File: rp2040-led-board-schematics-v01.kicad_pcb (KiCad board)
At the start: 4 copper layers, 228 x 98 mm, 293 parts, among them J1 ReceiverRS485, J10 Terminal, J11 ReceiverData, J12 ReceiverData, J13 ReceiverData, J14 ReceiverData, J15 ReceiverRS485, J16 ReceiverRS485, J17 ReceiverRS485, J18 ReceiverRS485, J19 Terminal, J2 ReceiverRS485, J20 Terminal, J21 Terminal, J22 Terminal, J23 ReceiverData, J24 ReceiverData, J25 ReceiverData, J26 ReceiverData, J27 MainBoard, J3 ReceiverRS485, J4 ReceiverRS485, J5 PWR_IN, J6 Terminal, J7 Terminal, J8 Terminal, J9 FrontPanel, Q1 AO3401A, SW1 PEC16, SW2 Button, U10 MAX485EE, U11 MAX485EE, U12 MAX485EE, U13 MAX485EE, U14 Pico, U15 MAX485EE, U16 MAX485EE, U17 AMS1117-5.0, U2 LMR50410Y5FQDBVRQ1, U21 MAX485EE, U22 MAX485EE, U23 MAX485EE, U24 MAX485EE, U25 MAX485EE, U26 MAX485EE, U27 ENC28J60, U29 AMS1117-5.0, U30 AMS1117-5.0, U31 AMS1117-5.0, U32 AMS1117-5.0, U33 AMS1117-5.0, U34 AMS1117-5.0, U35 AMS1117-5.0, U6 MAX485EE, U7 MAX485EE, U8 MAX485EE, U9 MAX485EE

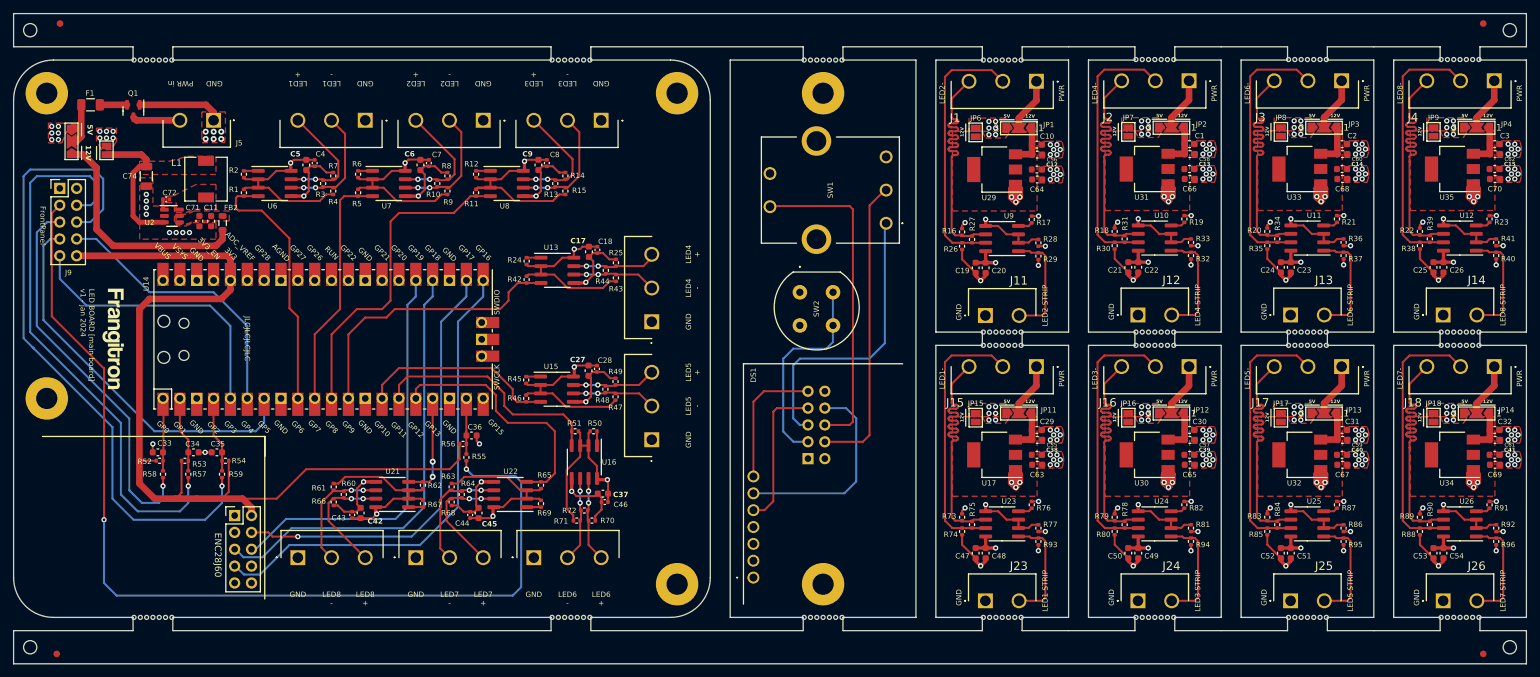
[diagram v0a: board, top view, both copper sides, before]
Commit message: remove designators from silkscreens (manufacturer considers different designs otherwise)
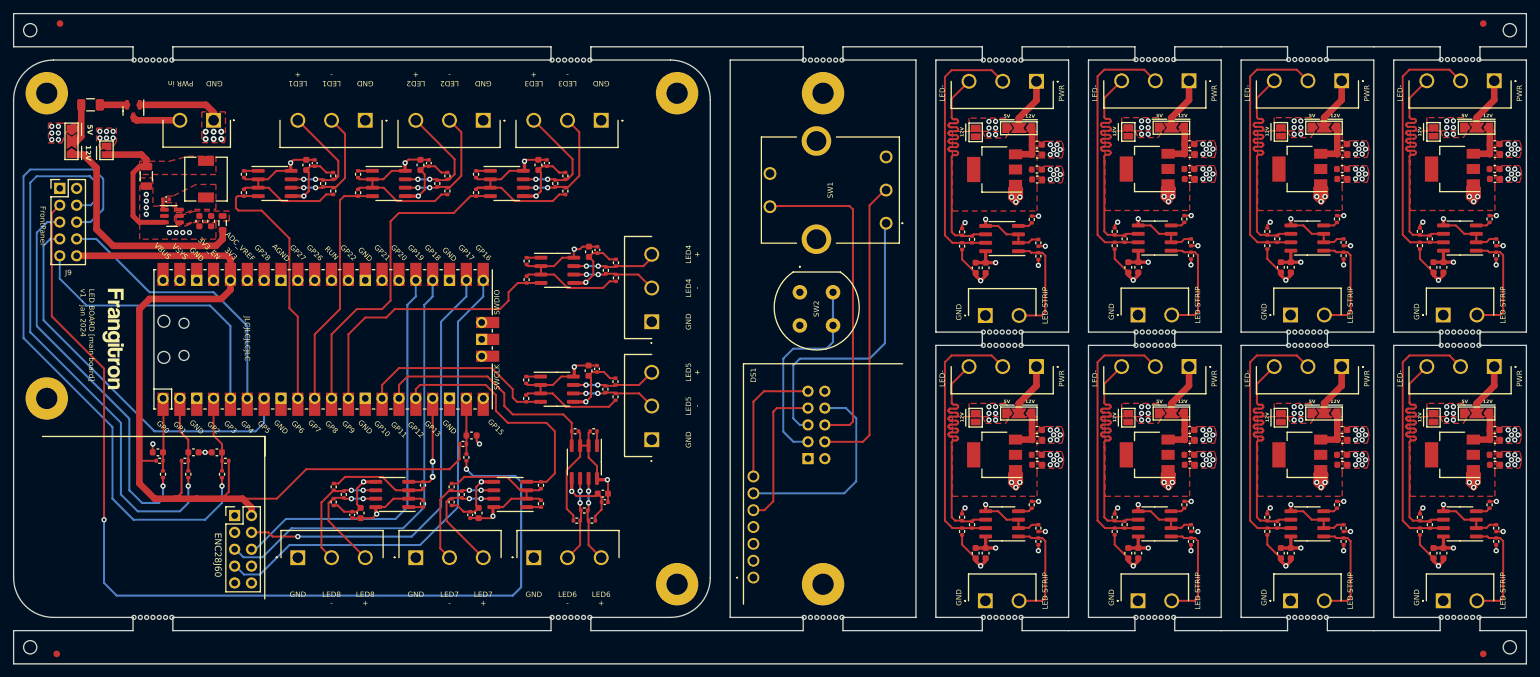
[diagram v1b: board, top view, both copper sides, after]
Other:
- board text added: "LED BOARD [receiver] v1 - jan 2024"
- board text added: "LED STRIP"
- board text added: "LED-"
- board text removed: "LED BOARD [receiver1] v1 - jan 2024"
- board text removed: "LED BOARD [receiver2] v1 - jan 2024"
- board text removed: "LED BOARD [receiver3] v1 - jan 2024"
- board text removed: "LED BOARD [receiver4] v1 - jan 2024"
- board text removed: "LED BOARD [receiver5] v1 - jan 2024"
- board text removed: "LED BOARD [receiver6] v1 - jan 2024"
- board text removed: "LED BOARD [receiver7] v1 - jan 2024"
- board text removed: "LED BOARD [receiver8] v1 - jan 2024"
- board text removed: "LED1 STRIP"
- board text removed: "LED1-"
- board text removed: "LED2 STRIP"
- board text removed: "LED2-"
- board text removed: "LED3 STRIP"
- board text removed: "LED3-"
- board text removed: "LED4 STRIP"
- board text removed: "LED4-"
- board text removed: "LED5 STRIP"
- board text removed: "LED5-"
- board text removed: "LED6 STRIP"
- board text removed: "LED6-"
- board text removed: "LED7 STRIP"
- board text removed: "LED7-"
- board text removed: "LED8 STRIP"
- board text removed: "LED8-"

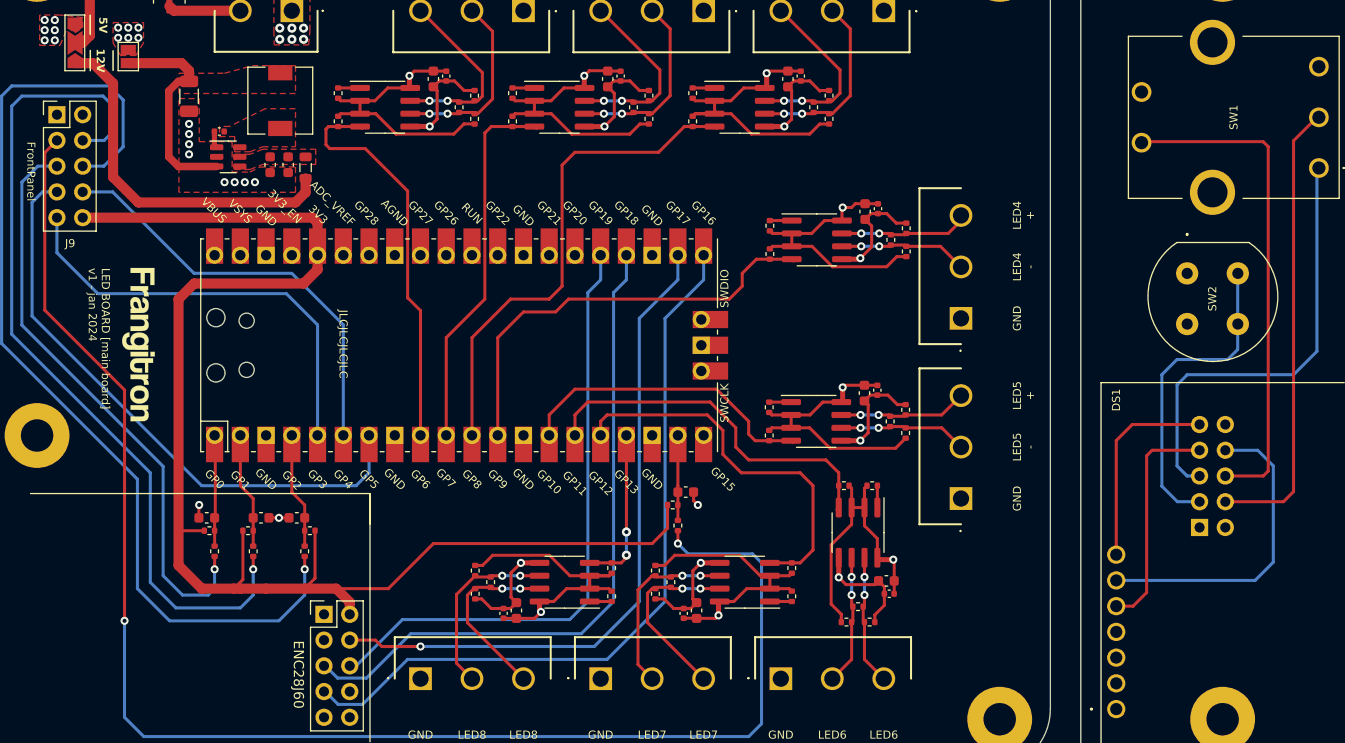
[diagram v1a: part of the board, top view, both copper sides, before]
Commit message: fix: remove designators from silkscreens (forgot some)
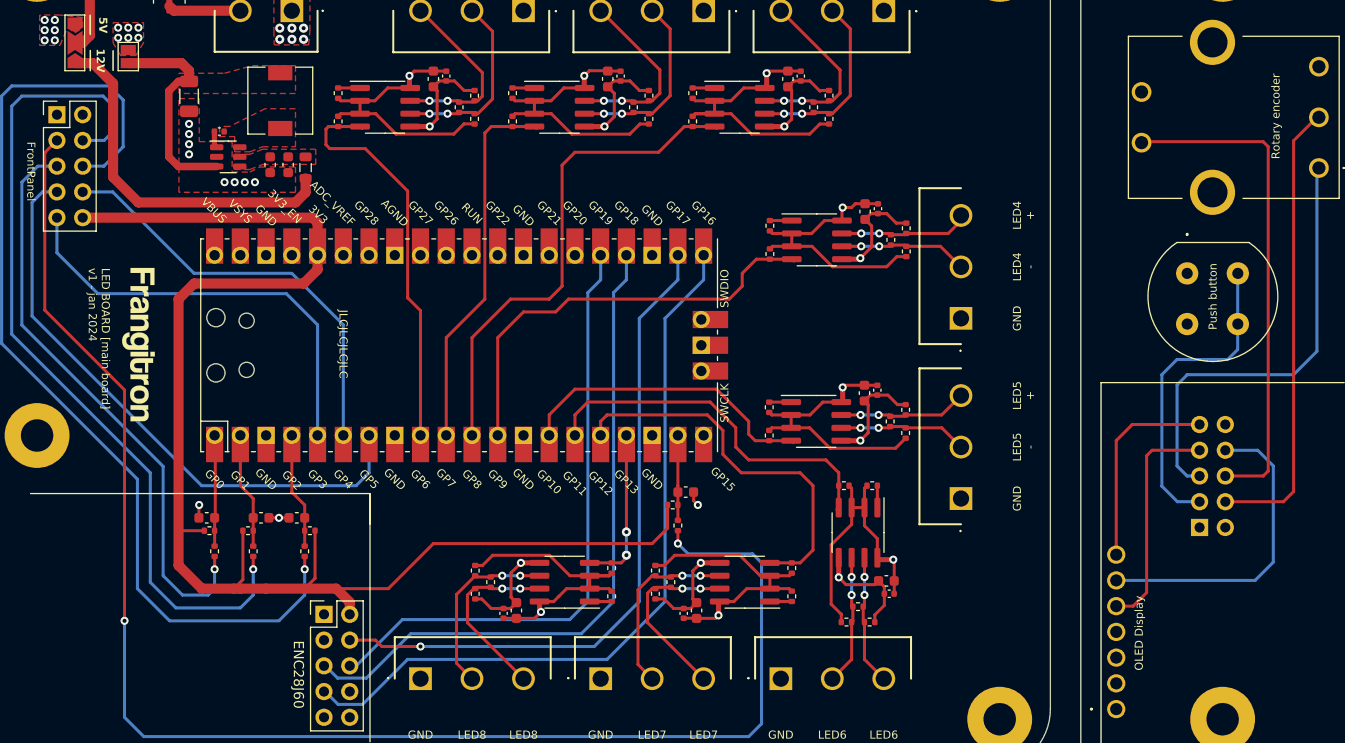
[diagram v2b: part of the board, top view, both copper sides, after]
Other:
- board text added: "OLED Display"
- board text added: "Push button"
- board text added: "Rotary encoder"
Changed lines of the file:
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@@
     (property "ki_keywords" "switch normally-open pushbutton push-button")
     (attr through_hole exclude_from_pos_files)
-    (fp_text reference "SW2" (at 2.5 -2.5 -90) (layer "F.SilkS")
+    (fp_text reference "SW2" (at 2.5 -2.5 -90) (layer "F.SilkS") hide
         (effects (font (size 0.8 0.8) (thickness 0.15)))
     )
@@
     (property "ki_description" "OLED Displays & Accessories")
     (attr through_hole exclude_from_pos_files)
-    (fp_text reference "DS1" (at 30.5 0 90) (layer "F.SilkS")
+    (fp_text reference "DS1" (at 30.5 0 90) (layer "F.SilkS") hide
         (effects (font (size 0.8 0.8) (thickness 0.15)))
     )
@@
     (property "ki_description" "Bourns Encoder 24ppr ppr 5 V dc")
     (attr through_hole exclude_from_pos_files)
-    (fp_text reference "SW1" (at 5 -8.4 90) (layer "F.SilkS")
+    (fp_text reference "SW1" (at 5 -8.4 90) (layer "F.SilkS") hide
         (effects (font (size 0.8 0.8) (thickness 0.15)))
     )
@@
         (effects (font (size 0.8 0.8) (thickness 0.15)))
     )
-    (fp_text user "${REFERENCE}" (at 1.3 12.7) (layer "F.SilkS")
-        (effects (font (size 0.8 0.8) (thickness 0.15)))
-    )
     (fp_line (start -1.33 -1.33) (end 0 -1.33)
       (stroke (width 0.12) (type solid)) (layer "F.SilkS"))
@@
     (effects (font (size 0.8 0.8) (thickness 0.15)) (justify top))
   )
+  (gr_text "Rotary encoder" (at 167.25 75.5 90) (layer "F.SilkS")
+    (effects (font (size 0.8 0.8) (thickness 0.15)))
+  )
   (gr_text "GND" (at 204.999998 137.000001 90) (layer "F.SilkS")
     (effects (font (size 0.8 0.8) (thickness 0.15)) (justify top))
@@
     (effects (font (size 0.5 0.5) (thickness 0.125) bold) (justify left bottom))
   )
+  (gr_text "OLED Display" (at 153.75 126.5 90) (layer "F.SilkS")
+    (effects (font (size 0.8 0.8) (thickness 0.15)))
+  )
   (gr_text "LED STRIP" (at 217.999998 92.925002 90) (layer "F.SilkS")
     (effects (font (size 0.8 0.8) (thickness 0.15)) (justify top))
@@
     (effects (font (size 0.5 0.5) (thickness 0.125) bold) (justify left bottom))
   )
+  (gr_text "Push button" (at 161.039999 93.286001 90) (layer "F.SilkS")
+    (effects (font (size 0.8 0.8) (thickness 0.15)))
+  )
   (gr_text "12V" (at 252.235999 67.507001 90) (layer "F.SilkS")
